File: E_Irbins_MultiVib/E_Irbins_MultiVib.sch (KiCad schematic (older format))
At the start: 11 parts, among them Q1 BC548, Q2 BC548

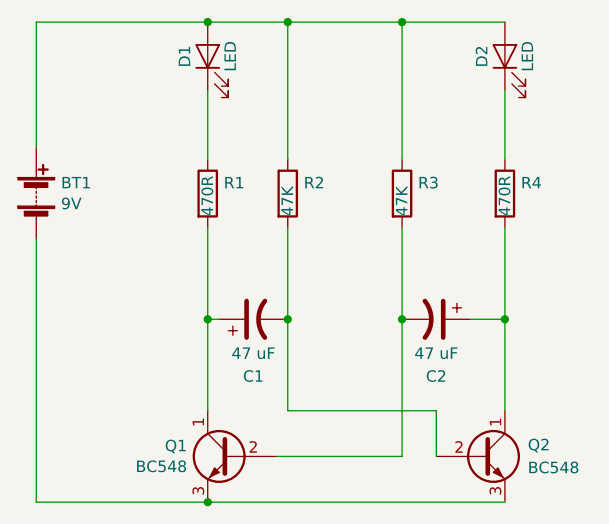
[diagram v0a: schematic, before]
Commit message: Tika izveidota jauna bibliotēka, kas satur pašizveidoto elektrisko komponenti (tranzistoru) BC846BS. Iepriekš pievienotā MultiVib shēma uzlabota, divus Tranzistorus aizvietojot ar jaunizveidoto mikroshēmu, kas sevī ietver divus NPN tranzistorus ar līdzīgiem parametriem.
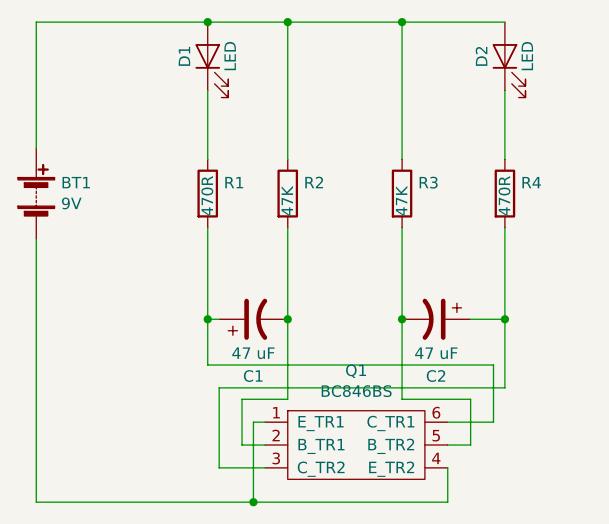
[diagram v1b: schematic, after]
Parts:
- removed Q1, Q2: BC548, Package_TO_SOT_THT:TO-92_Inline, symbol Transistor_BJT:BC548
- added Q1: BC846BS, symbol md_biblioteka(dual_NPN):BC846BS
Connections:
- net at BT1.2 (-): now also Q1.1 (E_TR1), Q1.4 (E_TR2)
- net at C2.1, R4.2: now also Q1.3 (C_TR2)
- net at C2.2, R3.2: now also Q1.5 (B_TR2)
- net at C1.2, R2.2: now also Q1.2 (B_TR1)
- net at C1.1, R1.2: now also Q1.6 (C_TR1)
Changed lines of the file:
@@
 EESchema Schematic File Version 4
-LIBS:E_Irbins_MultiVib-cache
 EELAYER 26 0
 EELAYER END
@@
 	0    1    1    0
 $EndComp
-$Comp
-L Transistor_BJT:BC548 Q1
-U 1 1 5C6E700C
-P 4550 4300
-F 0 "Q1" H 4740 4346 50  0000 L CNN
-F 1 "BC548" H 4740 4255 50  0000 L CNN
-F 2 "Package_TO_SOT_THT:TO-92_Inline" H 4750 4225 50  0001 L CIN
-F 3 "http://www.fairchildsemi.com/ds/BC/BC547.pdf" H 4550 4300 50  0001 L CNN
-	1    4550 4300
-	-1   0    0    -1
-$EndComp
-$Comp
-L Transistor_BJT:BC548 Q2
-U 1 1 5C6E7503
-P 5650 4300
-F 0 "Q2" H 5850 4350 50  0000 L CNN
-F 1 "BC548" H 5850 4250 50  0000 L CNN
-F 2 "Package_TO_SOT_THT:TO-92_Inline" H 5850 4225 50  0001 L CIN
-F 3 "http://www.fairchildsemi.com/ds/BC/BC547.pdf" H 5650 4300 50  0001 L CNN
-	1    5650 4300
-	1    0    0    -1
-$EndComp
 Wire Wire Line
 	3700 2950 3700 2400
@@
 Wire Wire Line
 	4450 3300 4450 3700
+Wire Wire Line
+	5600 3700 5750 3700
+Wire Wire Line
+	4450 3700 4500 3700
+Wire Wire Line
+	3700 3350 3700 4500
+Wire Wire Line
+	5300 2400 5750 2400
+Wire Wire Line
+	3700 2400 4450 2400
+Wire Wire Line
+	4800 2400 5300 2400
+$Comp
+L md_biblioteka(dual_NPN):BC846BS Q1
+U 1 1 5C8054CD
+P 5100 4250
+F 0 "Q1" H 5100 4575 50  0000 C CNN
+F 1 "BC846BS" H 5100 4484 50  0000 C CNN
+F 2 "" H 5100 4500 50  0001 C CNN
+F 3 "" H 5100 4500 50  0001 C CNN
+	1    5100 4250
+	1    0    0    -1
+$EndComp
+Wire Wire Line
+	4800 3700 4800 4050
+Wire Wire Line
+	4800 4050 4600 4050
+Wire Wire Line
+	4600 4050 4600 4250
+Wire Wire Line
+	4600 4250 4700 4250
 Connection ~ 4800 3700
+Wire Wire Line
+	5300 3700 5300 4050
+Wire Wire Line
+	5300 4050 5600 4050
+Wire Wire Line
+	5600 4050 5600 4250
+Wire Wire Line
+	5600 4250 5500 4250
 Connection ~ 5300 3700
 Wire Wire Line
-	5750 4100 5750 3700
-Wire Wire Line
-	5600 3700 5750 3700
-Wire Wire Line
-	4450 4100 4450 3700
+	4450 3700 4450 3900
+Wire Wire Line
+	4450 3900 5700 3900
+Wire Wire Line
+	5700 3900 5700 4150
+Wire Wire Line
+	5700 4150 5500 4150
 Connection ~ 4450 3700
 Wire Wire Line
-	4450 3700 4500 3700
-Wire Wire Line
-	4750 4300 5300 4300
-Wire Wire Line
-	5300 4300 5300 3700
-Wire Wire Line
-	5450 4300 5450 4100
-Wire Wire Line
-	5450 4100 4800 4100
-Wire Wire Line
-	4800 4100 4800 3700
-Wire Wire Line
-	3700 3350 3700 4500
+	5750 3700 5750 4000
+Wire Wire Line
+	5750 4000 4500 4000
+Wire Wire Line
+	4500 4000 4500 4350
+Wire Wire Line
+	4500 4350 4700 4350
 Connection ~ 5750 3700
 Wire Wire Line
-	3700 4500 4450 4500
-Wire Wire Line
-	5300 2400 5750 2400
-Wire Wire Line
-	3700 2400 4450 2400
-Wire Wire Line
-	4800 2400 5300 2400
-Wire Wire Line
-	4450 4500 5750 4500
-Connection ~ 4450 4500
+	3700 4500 4650 4500
+Wire Wire Line
+	4650 4500 4650 4150
+Wire Wire Line
+	4650 4150 4700 4150
+Wire Wire Line
+	4650 4500 5500 4500
+Wire Wire Line
+	5500 4500 5500 4350
+Connection ~ 4650 4500
 $EndSCHEMATC
